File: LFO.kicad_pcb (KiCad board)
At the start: 4 copper layers, 29.5 x 106.5 mm, 102 parts, among them J1 AudioJack2_SwitchT, J2 AudioJack2_SwitchT, J3 AudioJack2_SwitchT, J4 AudioJack2_SwitchT, J5 AudioJack2_SwitchT, J6 AudioJack2_SwitchT, J7 Conn_02x03_Odd_Even, J8 Conn_02x05_Odd_Even, Q1 BC847, SW1 SW_Push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

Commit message: Ground vias for MCU.
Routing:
- net GND: vias 32 -> 38
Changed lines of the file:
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@@
     (thickness 1.6)
     (drawings 75)
-    (tracks 741)
+    (tracks 747)
     (zones 0)
     (modules 102)
@@
   )
   (gr_line (start 145.706 67.916) (end 141.134 67.916) (layer B.SilkS) (width 0.4))
+  (via (at 148.119 98.269) (size 0.8) (drill 0.4) (layers F.Cu B.Cu) (net 65))
+  (via (at 149.389 98.269) (size 0.8) (drill 0.4) (layers F.Cu B.Cu) (net 65))
+  (via (at 149.389 96.999) (size 0.8) (drill 0.4) (layers F.Cu B.Cu) (net 65))
+  (via (at 148.119 96.999) (size 0.8) (drill 0.4) (layers F.Cu B.Cu) (net 65))
   (segment (start 154.53 86.0267) (end 155.4024 86.0267) (width 0.25) (layer B.Cu) (net 1))
   (segment (start 154.53 86.882) (end 154.53 86.0267) (width 0.25) (layer B.Cu) (net 1))
@@
   (via (at 145.452 93.316) (size 0.8) (drill 0.4) (layers F.Cu B.Cu) (net 65))
   (via (at 143.674 101.19) (size 0.8) (drill 0.4) (layers F.Cu B.Cu) (net 65))
+  (via (at 149.389 56.994) (size 0.8) (drill 0.4) (layers F.Cu B.Cu) (net 65))
+  (via (at 151.675 56.994) (size 0.8) (drill 0.4) (layers F.Cu B.Cu) (net 65))
   (segment (start 159.6505 141.322) (end 159.6505 138.832) (width 0.25) (layer B.Cu) (net 66))
   (segment (start 159.6505 138.832) (end 159.6255 138.807) (width 0.25) (layer B.Cu) (net 66))

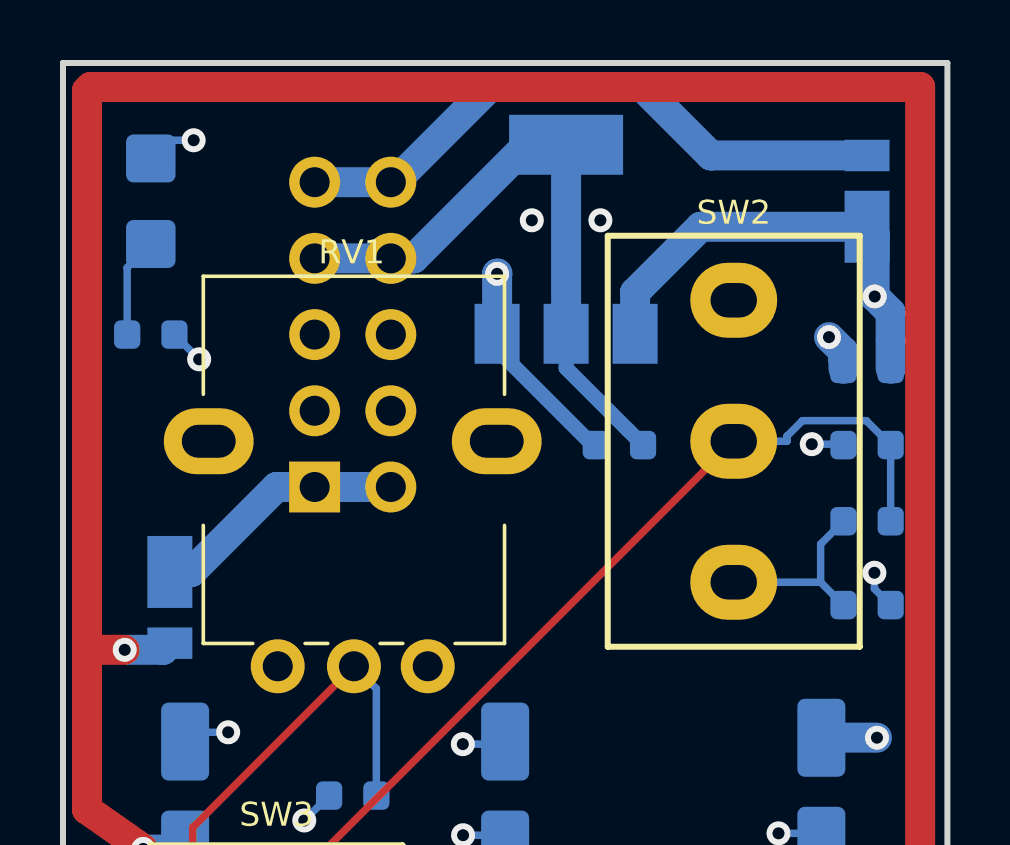
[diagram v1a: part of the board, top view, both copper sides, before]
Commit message: Double power vias.
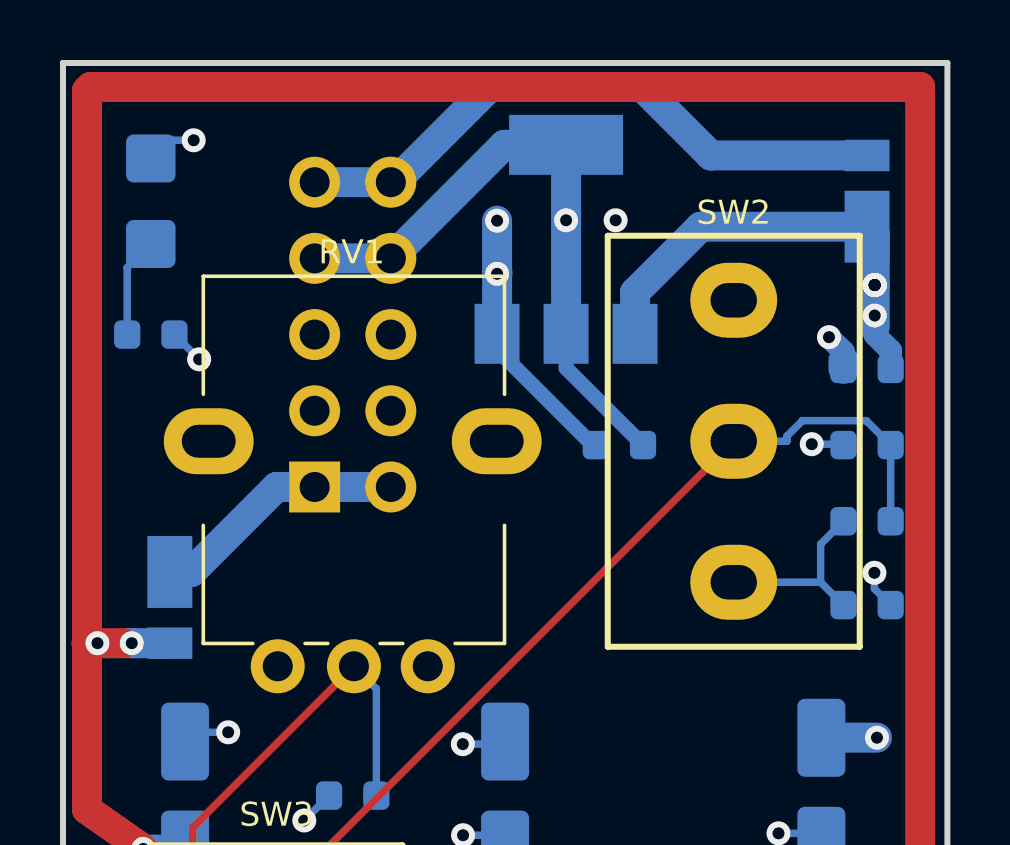
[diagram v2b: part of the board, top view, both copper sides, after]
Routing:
- net +5V: track 24.9 -> 26.7 mm, vias 13 -> 14
- net -12V: track 153.4 -> 154.2 mm, vias 5 -> 6
- net +12V: track 108.7 -> 109.2 mm, vias 3 -> 6
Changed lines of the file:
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@@
     (thickness 1.6)
     (drawings 75)
-    (tracks 747)
+    (tracks 756)
     (zones 0)
     (modules 102)
@@
   )
   (setup
-    (last_trace_width 0.25)
+    (last_trace_width 1)
     (user_trace_width 0.4)
     (user_trace_width 0.5)
@@
     (solder_mask_min_width 0.25)
     (aux_axis_origin 148.5 105)
-    (grid_origin 148.5 105)
     (visible_elements FFFFFF7F)
     (pcbplotparams
@@
   (via (at 158.7208 64.4575) (size 0.8) (layers F.Cu B.Cu) (net 1))
   (via (at 148.232 58.779) (size 0.8) (layers F.Cu B.Cu) (net 1))
+  (segment (start 148.232 58.779) (end 148.232 57.008) (width 1) (layer B.Cu) (net 1))
+  (via (at 148.232 57.008) (size 0.8) (drill 0.4) (layers F.Cu B.Cu) (net 1))
   (segment (start 159.6505 128.698) (end 158.7065 129.642) (width 0.25) (layer B.Cu) (net 2))
   (segment (start 158.7065 129.642) (end 157.4555 129.642) (width 0.25) (layer B.Cu) (net 2))
   (segment (start 159.625 127.504) (end 159.6505 127.5295) (width 0.25) (layer B.Cu) (net 2))
   (segment (start 159.6505 127.5295) (end 159.6505 128.698) (width 0.25) (layer B.Cu) (net 2))
-  (segment (start 161.352 61.0072) (end 161.3525 61.0077) (width 0.25) (layer B.Cu) (net 2))
-  (segment (start 161.3525 61.0077) (end 161.3525 61.947) (width 0.25) (layer B.Cu) (net 2))
-  (segment (start 161.352 61.0072) (end 161.352 61.947) (width 1) (layer B.Cu) (net 2))
-  (segment (start 160.819 59.534) (end 161.352 60.0675) (width 1) (layer B.Cu) (net 2))
-  (segment (start 161.352 60.0675) (end 161.352 61.0072) (width 1) (layer B.Cu) (net 2))
   (segment (start 162.216 75.5614) (end 160.895 74.2406) (width 1) (layer In1.Cu) (net 2))
   (segment (start 161.733 110.842) (end 161.733 109.648) (width 1) (layer In1.Cu) (net 2))
@@
   (segment (start 155.016 57.209) (end 152.832 59.393) (width 1) (layer B.Cu) (net 2))
   (segment (start 152.832 59.393) (end 152.832 60.779) (width 1) (layer B.Cu) (net 2))
-  (segment (start 160.819 59.534) (end 160.819 57.463) (width 1) (layer B.Cu) (net 2))
-  (segment (start 160.819 57.463) (end 160.565 57.209) (width 1) (layer B.Cu) (net 2))
-  (segment (start 162.216 75.5614) (end 162.216 60.931) (width 1) (layer In1.Cu) (net 2))
-  (segment (start 162.216 60.931) (end 160.819 59.534) (width 1) (layer In1.Cu) (net 2))
   (segment (start 160.895 74.2406) (end 159.044 74.2406) (width 1) (layer B.Cu) (net 2))
   (segment (start 159.044 74.2406) (end 159.041 74.244) (width 1) (layer B.Cu) (net 2))
   (via (at 159.625 127.504) (size 0.8) (layers F.Cu B.Cu) (net 2))
-  (via (at 160.819 59.534) (size 0.8) (layers F.Cu B.Cu) (net 2))
   (via (at 160.895 74.2406) (size 0.8) (layers F.Cu B.Cu) (net 2))
+  (segment (start 160.819 57.463) (end 160.565 57.209) (width 1) (layer B.Cu) (net 2))
+  (via (at 160.819 59.153) (size 0.8) (drill 0.4) (layers F.Cu B.Cu) (net 2))
+  (segment (start 160.819 59.153) (end 160.819 57.463) (width 1) (layer B.Cu) (net 2))
+  (segment (start 162.216 60.931) (end 162.216 75.5614) (width 1) (layer In1.Cu) (net 2))
+  (segment (start 160.819 59.153) (end 160.819 60.55) (width 1) (layer B.Cu) (net 2))
+  (via (at 160.819 59.153) (size 0.8) (drill 0.4) (layers F.Cu B.Cu) (net 2))
+  (via (at 160.819 59.153) (size 0.8) (drill 0.4) (layers F.Cu B.Cu) (net 2))
+  (via (at 160.819 60.169) (size 0.8) (drill 0.4) (layers F.Cu B.Cu) (net 2))
+  (segment (start 161.562857 60.169) (end 161.816857 60.423) (width 1) (layer In1.Cu) (net 2))
+  (segment (start 160.819 60.169) (end 161.562857 60.169) (width 1) (layer In1.Cu) (net 2))
+  (segment (start 160.819 59.153) (end 161.816857 60.423) (width 1) (layer In1.Cu) (net 2))
+  (segment (start 161.816857 60.423) (end 162.216 60.931) (width 1) (layer In1.Cu) (net 2))
+  (segment (start 160.819 60.804) (end 160.819 60.55) (width 0.75) (layer B.Cu) (net 2))
+  (segment (start 161.3525 61.947) (end 161.3525 61.3375) (width 0.75) (layer B.Cu) (net 2))
+  (segment (start 161.3525 61.3375) (end 160.819 60.804) (width 0.75) (layer B.Cu) (net 2))
   (segment (start 157.324 152.074) (end 157.324 152.9293) (width 0.25) (layer B.Cu) (net 3))
   (segment (start 155.5865 155.165) (end 155.5865 154.6668) (width 0.25) (layer B.Cu) (net 3))
@@
   (segment (start 152.31 128.495) (end 152.31 129.511) (width 1) (layer B.Cu) (net 25))
   (segment (start 158.62 112.5) (end 158.431 112.311) (width 1) (layer In1.Cu) (net 25))
-  (segment (start 135.819 71.3128) (end 137.103 71.3128) (width 1) (layer B.Cu) (net 25))
-  (segment (start 137.103 71.3128) (end 137.324 71.092) (width 1) (layer B.Cu) (net 25))
-  (segment (start 134.562 71.3128) (end 135.819 71.3128) (width 1) (layer F.Cu) (net 25))
+  (segment (start 134.543 71.091) (end 135.8 71.091) (width 1) (layer F.Cu) (net 25))
   (via (at 146.57 125.93) (size 0.8) (layers F.Cu B.Cu) (net 25))
   (via (at 158.095 122.659) (size 0.8) (layers F.Cu B.Cu) (net 25))
   (via (at 136.435 77.949) (size 0.8) (layers F.Cu B.Cu) (net 25))
   (via (at 152.31 128.495) (size 0.8) (layers F.Cu B.Cu) (net 25))
-  (via (at 135.819 71.3128) (size 0.8) (layers F.Cu B.Cu) (net 25))
+  (via (at 136.054 71.091) (size 0.8) (layers F.Cu B.Cu) (net 25))
   (segment (start 159.326 113.206) (end 158.62 112.5) (width 1) (layer F.Cu) (net 25))
   (segment (start 158.095 122.659) (end 159.326 121.428) (width 1) (layer F.Cu) (net 25))
   (segment (start 159.326 121.428) (end 159.326 113.206) (width 1) (layer F.Cu) (net 25))
+  (segment (start 136.055 71.092) (end 136.054 71.091) (width 1) (layer B.Cu) (net 25))
+  (segment (start 137.324 71.092) (end 136.055 71.092) (width 1) (layer B.Cu) (net 25))
+  (via (at 134.911 71.091) (size 0.8) (drill 0.4) (layers F.Cu B.Cu) (net 25))
+  (segment (start 136.054 71.091) (end 134.911 71.091) (width 1) (layer B.Cu) (net 25))
   (segment (start 159.6505 131.035) (end 157.8485 131.035) (width 0.25) (layer B.Cu) (net 26))
   (segment (start 157.8485 131.035) (end 157.4555 130.642) (width 0.25) (layer B.Cu) (net 26))
@@
   (segment (start 159.778 61.6595) (end 159.7775 61.66) (width 0.25) (layer B.Cu) (net 65))
   (segment (start 159.7775 61.66) (end 159.7775 61.947) (width 0.25) (layer B.Cu) (net 65))
-  (segment (start 159.778 61.6595) (end 159.778 61.372) (width 1) (layer B.Cu) (net 65))
-  (segment (start 159.778 61.372) (end 159.295 60.8895) (width 1) (layer B.Cu) (net 65))
   (segment (start 159.778 61.947) (end 159.778 61.6595) (width 1) (layer B.Cu) (net 65))
   (segment (start 148.754 99.5715) (end 148.754 97.634) (width 0.25) (layer B.Cu) (net 65))
@@
   (segment (start 139.268 74.0605) (end 138.1425 74.0605) (width 0.25) (layer B.Cu) (net 65))
   (segment (start 138.1425 74.0605) (end 137.832 74.371) (width 0.25) (layer B.Cu) (net 65))
-  (segment (start 144.69 58.264) (end 145.452 58.264) (width 1) (layer B.Cu) (net 65))
-  (segment (start 145.452 58.264) (end 149.237 54.479) (width 1) (layer B.Cu) (net 65))
-  (segment (start 149.237 54.479) (end 150.532 54.479) (width 1) (layer B.Cu) (net 65))
   (segment (start 142.15 58.264) (end 144.69 58.264) (width 1) (layer B.Cu) (net 65))
   (segment (start 150.532 60.779) (end 150.532 54.479) (width 1) (layer B.Cu) (net 65))
@@
   (via (at 145.452 93.316) (size 0.8) (drill 0.4) (layers F.Cu B.Cu) (net 65))
   (via (at 143.674 101.19) (size 0.8) (drill 0.4) (layers F.Cu B.Cu) (net 65))
-  (via (at 149.389 56.994) (size 0.8) (drill 0.4) (layers F.Cu B.Cu) (net 65))
-  (via (at 151.675 56.994) (size 0.8) (drill 0.4) (layers F.Cu B.Cu) (net 65))
+  (via (at 152.183 56.994) (size 0.8) (drill 0.4) (layers F.Cu B.Cu) (net 65))
+  (via (at 150.532 56.994) (size 0.8) (drill 0.4) (layers F.Cu B.Cu) (net 65))
+  (segment (start 149.237 54.479) (end 150.532 54.479) (width 1) (layer B.Cu) (net 65))
+  (segment (start 144.69 58.264) (end 148.475 54.479) (width 1) (layer B.Cu) (net 65))
+  (segment (start 148.475 54.479) (end 149.237 54.479) (width 1) (layer B.Cu) (net 65))
+  (segment (start 159.7775 61.372) (end 159.295 60.8895) (width 0.75) (layer B.Cu) (net 65))
+  (segment (start 159.7775 61.947) (end 159.7775 61.372) (width 0.75) (layer B.Cu) (net 65))
   (segment (start 159.6505 141.322) (end 159.6505 138.832) (width 0.25) (layer B.Cu) (net 66))
   (segment (start 159.6505 138.832) (end 159.6255 138.807) (width 0.25) (layer B.Cu) (net 66))
